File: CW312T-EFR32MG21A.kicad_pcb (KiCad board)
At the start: 2 copper layers, 58.7 x 53.7 mm, 22 parts, among them J1 1x3 straight header pins, P1 PCIEx4 EDGE CONNECTOR, U1 EFR32MG21A020F1024IM32-BR

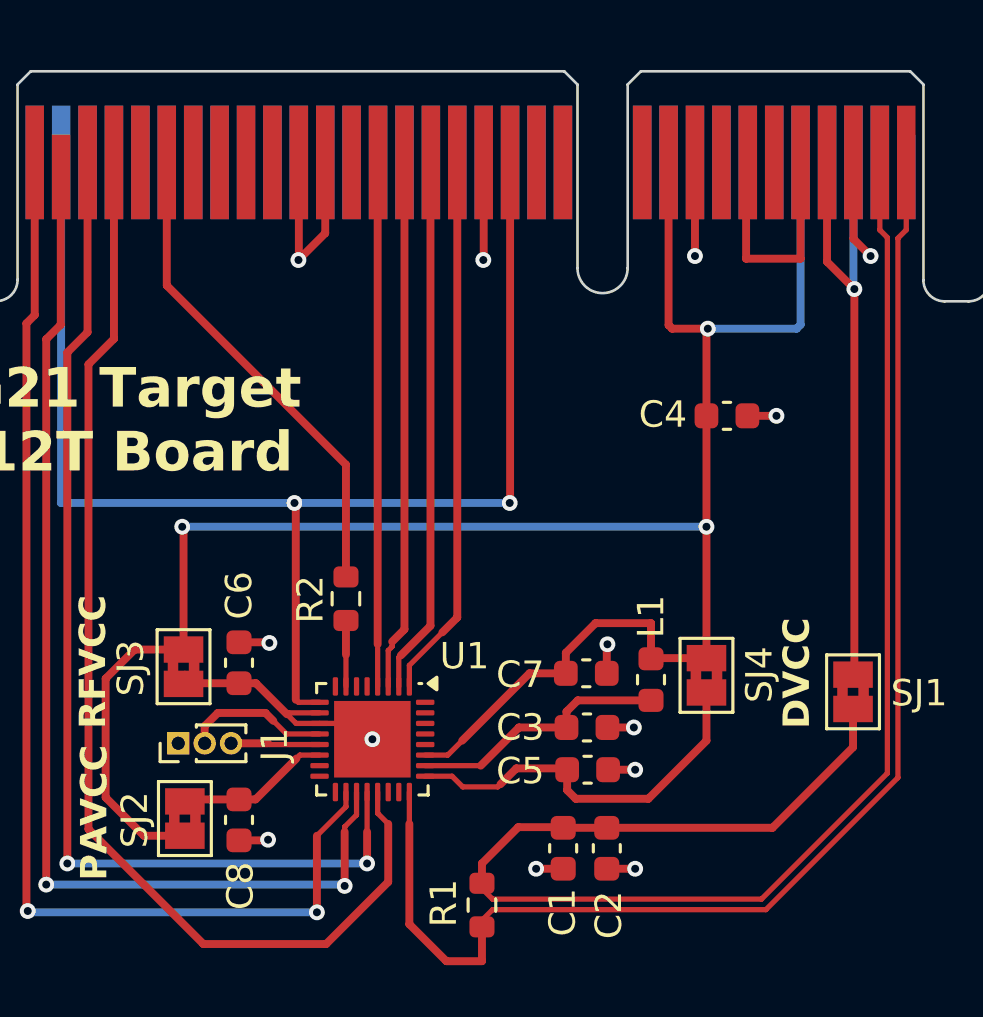
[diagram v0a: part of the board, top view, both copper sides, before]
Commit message: updated schematic to fix power, updated pcb and production files - ready for review
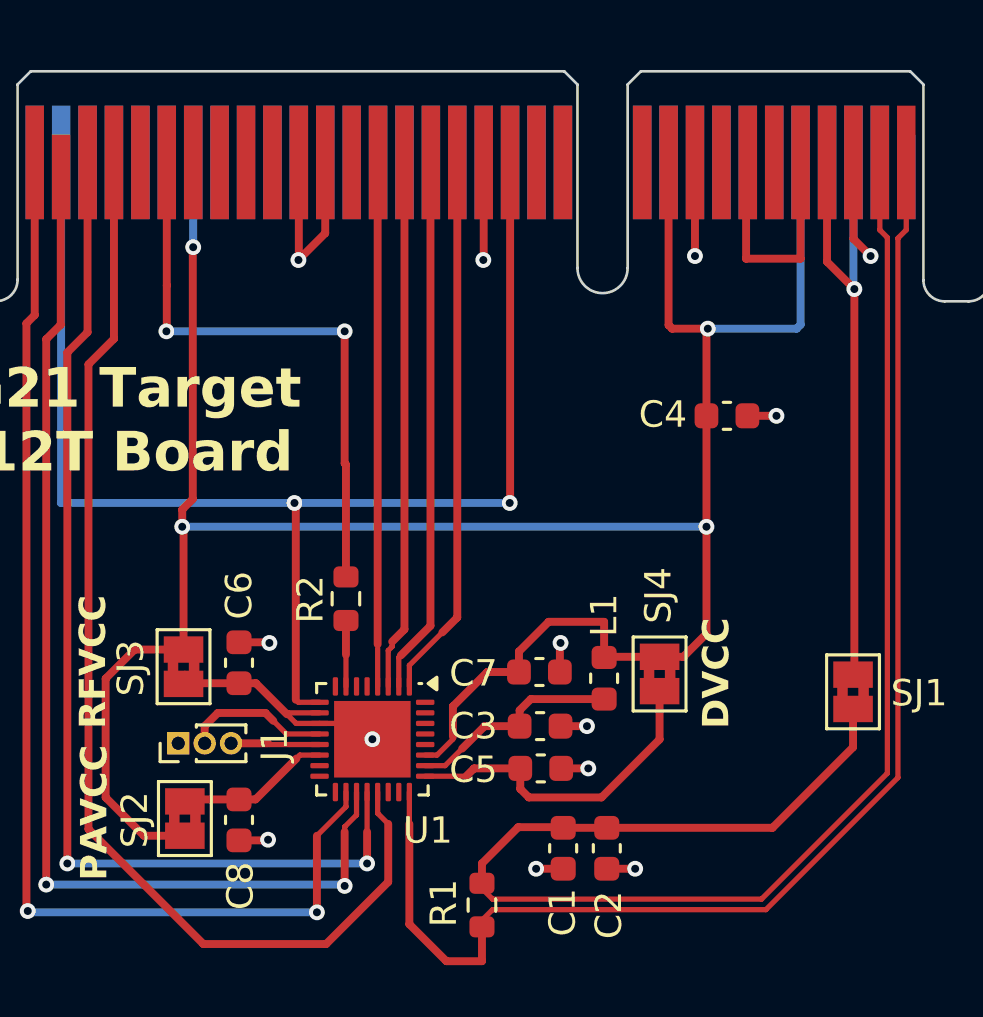
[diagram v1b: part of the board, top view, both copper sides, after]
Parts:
- moved C5 1.78 mm to (135.2, 90.3)
- moved C3 1.78 mm to (135.2, 88.8)
- moved C7 1.78 mm to (135.2, 86.7)
- moved L1 1.78 mm to (137.6, 86.9)
- moved SJ4 1.78 mm to (139.7, 86.8)
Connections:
- P1 pad A26: unconnected-(P1-JTAG_VREF-PadA26) -> +3V3
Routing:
- net +3V3: track 80.5 -> 94.6 mm, vias 3 -> 4
- net Net-(P1-CLKOUT): track 18.5 -> 22.5 mm, vias 0 -> 2
- net Net-(U1-DVDD): track 14.9 -> 12.9 mm
- net Net-(U1-AVDD): track 9.93 -> 8.17 mm

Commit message: updated silkscreen and production files
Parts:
- moved C4 1.75 mm to (142.3, 78.8)
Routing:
- net +3V3: track 94.6 -> 93.1 mm
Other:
- board text added: "+1V2"
- board text added: "+3V3"
- board text added: "Enable Supplies"
- board text added: "RST"
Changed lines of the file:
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@@
 	(footprint "Capacitor_SMD:C_0603_1608Metric"
 		(layer "F.Cu")
-		(at 142.275 77 180)
+		(at 142.35 78.75 180)
 		(descr "Capacitor SMD 0603 (1608 Metric), square (rectangular) end terminal, IPC_7351 nominal, (Body size source: IPC-SM-782 page 76, https://www.pcb-3d.com/wordpress/wp-content/uploads/ipc-sm-782a_amendment_1_and_2.pdf), generated with kicad-footprint-generator")
 		(tags "capacitor")
@@
 		)
 	)
+	(gr_line
+		(start 117.05 69.9)
+		(end 117.05 70.9)
+		(stroke
+			(width 0.15)
+			(type default)
+		)
+		(layer "B.SilkS")
+	)
 	(gr_rect
 		(start 154.75 103.2)
@@
 		(layer "F.SilkS")
 	)
+	(gr_line
+		(start 143 69.9)
+		(end 143 70.9)
+		(stroke
+			(width 0.15)
+			(type default)
+		)
+		(layer "F.SilkS")
+	)
 	(gr_rect
 		(start 154.75 105.35)
@@
 		(layer "F.SilkS")
 	)
+	(gr_line
+		(start 140.05 69.9)
+		(end 140.05 70.9)
+		(stroke
+			(width 0.15)
+			(type default)
+		)
+		(layer "F.SilkS")
+	)
 	(gr_text "NewAE Technology Inc. \nCW312T-EFR32MG21\nRoHS / Pb Free"
 		(at 131.05 88.2 0)
@@
 		)
 	)
+	(gr_text "RST"
+		(at 116.35 73.6 -90)
+		(layer "B.SilkS")
+		(effects
+			(font
+				(size 1 1)
+				(thickness 0.15)
+			)
+			(justify left bottom mirror)
+		)
+	)
 	(gr_text "B: Secure Vault"
 		(at 147.6 110.9 0)
@@
 		)
 	)
+	(gr_text "Enable Supplies"
+		(at 135.65 76.85 0)
+		(layer "F.SilkS")
+		(effects
+			(font
+				(size 1 1)
+				(thickness 0.15)
+			)
+			(justify left bottom)
+		)
+	)
 	(gr_text "DVCC"
 		(at 142.45 88.85 90)
@@
 		)
 	)
+	(gr_text "+3V3"
+		(at 139.4 71 270)
+		(layer "F.SilkS")
+		(effects
+			(font
+				(size 1 1)
+				(thickness 0.15)
+			)
+			(justify left bottom)
+		)
+	)
+	(gr_text "+1V2"
+		(at 142.35 71 270)
+		(layer "F.SilkS")
+		(effects
+			(font
+				(size 1 1)
+				(thickness 0.15)
+			)
+			(justify left bottom)
+		)
+	)
 	(gr_text "A: Std. Security"
 		(at 147.75 109.25 0)
@@
 	)
 	(segment
-		(start 143.05 77)
-		(end 144.15 77)
+		(start 143.15 78.75)
+		(end 144.25 78.75)
 		(width 0.3)
 		(layer "F.Cu")
@@
 	)
 	(via
-		(at 144.15 77)
+		(at 144.25 78.75)
 		(size 0.6)
 		(drill 0.3)
@@
 	)
 	(segment
-		(start 140.2 73.7)
-		(end 140.065 73.565)
+		(start 140.2 72.2)
+		(end 140.065 72.065)
 		(width 0.3)
 		(layer "F.Cu")
@@
 	)
 	(segment
-		(start 141.55 73.7)
-		(end 140.2 73.7)
-		(width 0.3)
-		(layer "F.Cu")
-		(net 4)
-	)
-	(segment
-		(start 141.5 73.75)
-		(end 141.55 73.7)
+		(start 141.55 72.2)
+		(end 140.2 72.2)
 		(width 0.3)
 		(layer "F.Cu")
@@
 	)
 	(segment
-		(start 141.5 77)
-		(end 141.5 73.75)
+		(start 141.5 72.25)
+		(end 141.55 72.2)
 		(width 0.3)
 		(layer "F.Cu")
@@
 	)
 	(segment
-		(start 141.5 77)
-		(end 141.5 81.2)
-		(width 0.3)
+		(start 137.649996 86.125004)
+		(end 137.625 86.15)
+		(width 0.2)
 		(layer "F.Cu")
 		(net 4)
 	)
 	(segment
-		(start 137.649996 86.125004)
-		(end 137.625 86.15)
-		(width 0.2)
+		(start 141.5 81.2)
+		(end 141.5 72.25)
+		(width 0.3)
 		(layer "F.Cu")
 		(net 4)
@@
 	)
 	(segment
-		(start 140.065 73.565)
-		(end 140.065 67.405)
+		(start 122.05 80.15)
+		(end 121.65 80.55)
 		(width 0.3)
 		(layer "F.Cu")
@@
 	)
 	(segment
-		(start 122.05 80.15)
-		(end 121.65 80.55)
+		(start 140.065 72.065)
+		(end 140.065 67.405)
 		(width 0.3)
 		(layer "F.Cu")
@@
 	)
 	(via
-		(at 141.55 73.7)
+		(at 141.55 72.2)
 		(size 0.6)
 		(drill 0.3)
@@
 	)
 	(segment
-		(start 145.065 73.55)
+		(start 145.065 72.05)
 		(end 145.065 67.405)
 		(width 0.3)
@@
 	)
 	(segment
-		(start 144.915 73.7)
-		(end 145.065 73.55)
+		(start 144.915 72.2)
+		(end 145.065 72.05)
 		(width 0.3)
 		(layer "B.Cu")
@@
 	)
 	(segment
-		(start 141.55 73.7)
-		(end 144.915 73.7)
+		(start 141.55 72.2)
+		(end 144.915 72.2)
 		(width 0.3)
 		(layer "B.Cu")
@@
 	)
 	(segment
-		(start 121.065 72.065)
-		(end 121.065 73.785)
-		(width 0.3)
-		(layer "F.Cu")
-		(net 31)
-	)
-	(segment
-		(start 127.8 78.8)
-		(end 127.85 78.85)
+		(start 127.85 73.85)
+		(end 127.85 83.1)
 		(width 0.3)
 		(layer "F.Cu")
@@
 	)
 	(segment
-		(start 121.065 73.785)
-		(end 121.05 73.8)
+		(start 121.065 72.065)
+		(end 121.065 73.785)
 		(width 0.3)
 		(layer "F.Cu")
@@
 	)
 	(segment
-		(start 127.85 78.85)
-		(end 127.85 83.1)
+		(start 127.8 73.8)
+		(end 127.85 73.85)
 		(width 0.3)
 		(layer "F.Cu")
@@
 	)
 	(segment
-		(start 127.8 73.8)
-		(end 127.8 78.8)
+		(start 121.065 73.785)
+		(end 121.05 73.8)
 		(width 0.3)
 		(layer "F.Cu")

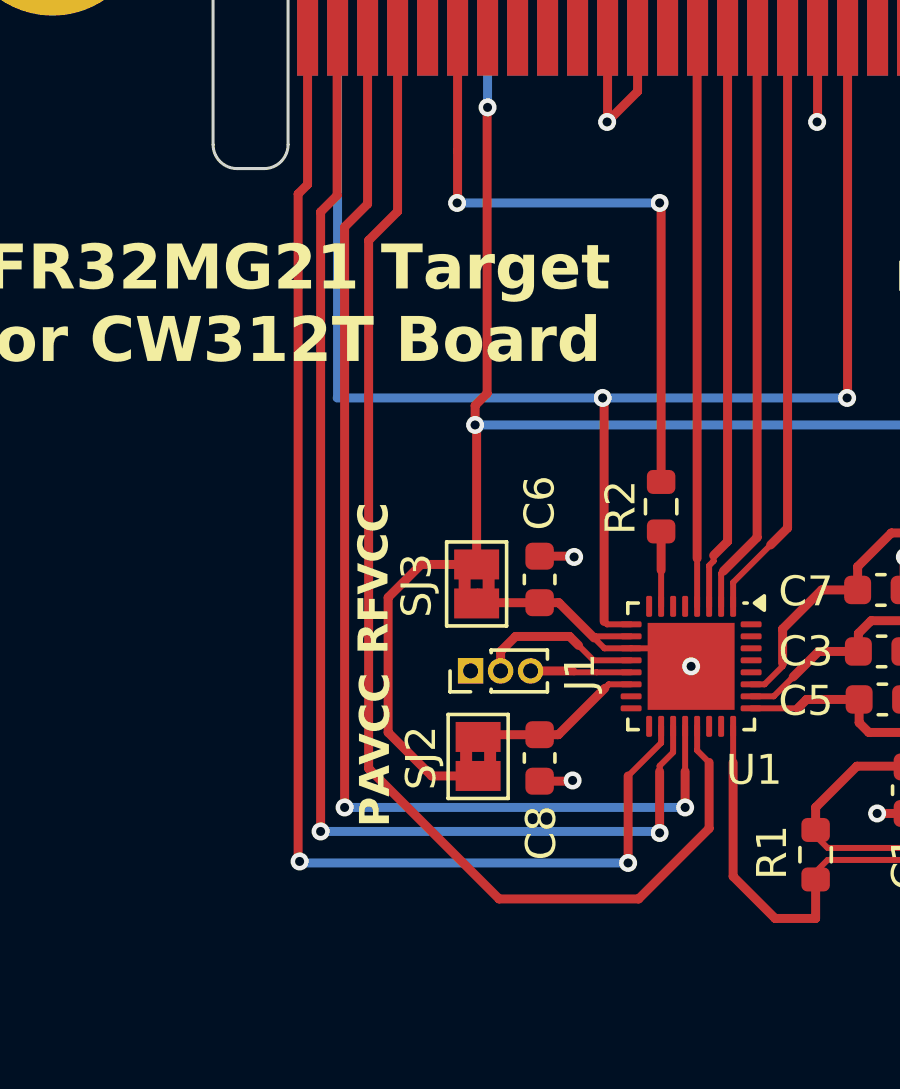
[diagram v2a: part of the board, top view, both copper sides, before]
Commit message: updated 3 pin header to fix footprint
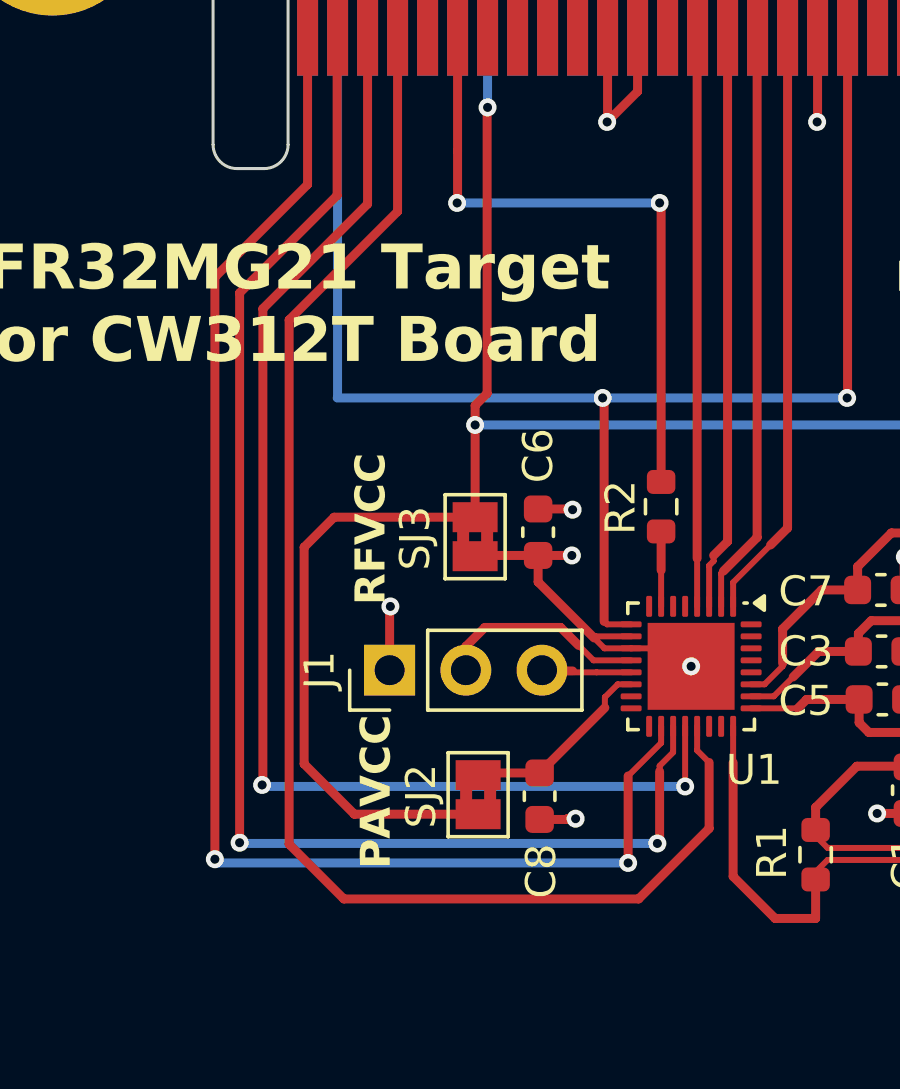
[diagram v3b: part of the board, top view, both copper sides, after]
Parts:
- J1: footprint Connector_PinHeader_1.00mm:PinHeader_1x03_P1.00mm_Vertical -> Connector_PinHeader_2.54mm:PinHeader_1x03_P2.54mm_Vertical
- moved J1 2.70 mm to (118.8, 89.4)
- moved C6 1.58 mm to (123.8, 84.8)
- moved SJ3 1.58 mm to (121.7, 84.9)
- moved C8 1.28 mm to (123.8, 93.6)
- moved SJ2 1.28 mm to (121.8, 93.5)
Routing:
- net +3V3: track 93.1 -> 99.9 mm
- net /TDI: track 43.3 -> 48.6 mm
- net GND: track 36.9 -> 41.4 mm, vias 13 -> 15
- net /SWDIO: track 42.1 -> 46.6 mm
- net /SWCLK: track 44.5 -> 48.4 mm
- net /TDO: track 40.9 -> 43.4 mm
- net Net-(U1-RF2G4_IO2): track 5.49 -> 7.02 mm
- net Net-(U1-PAVDD): track 5.83 -> 6.45 mm

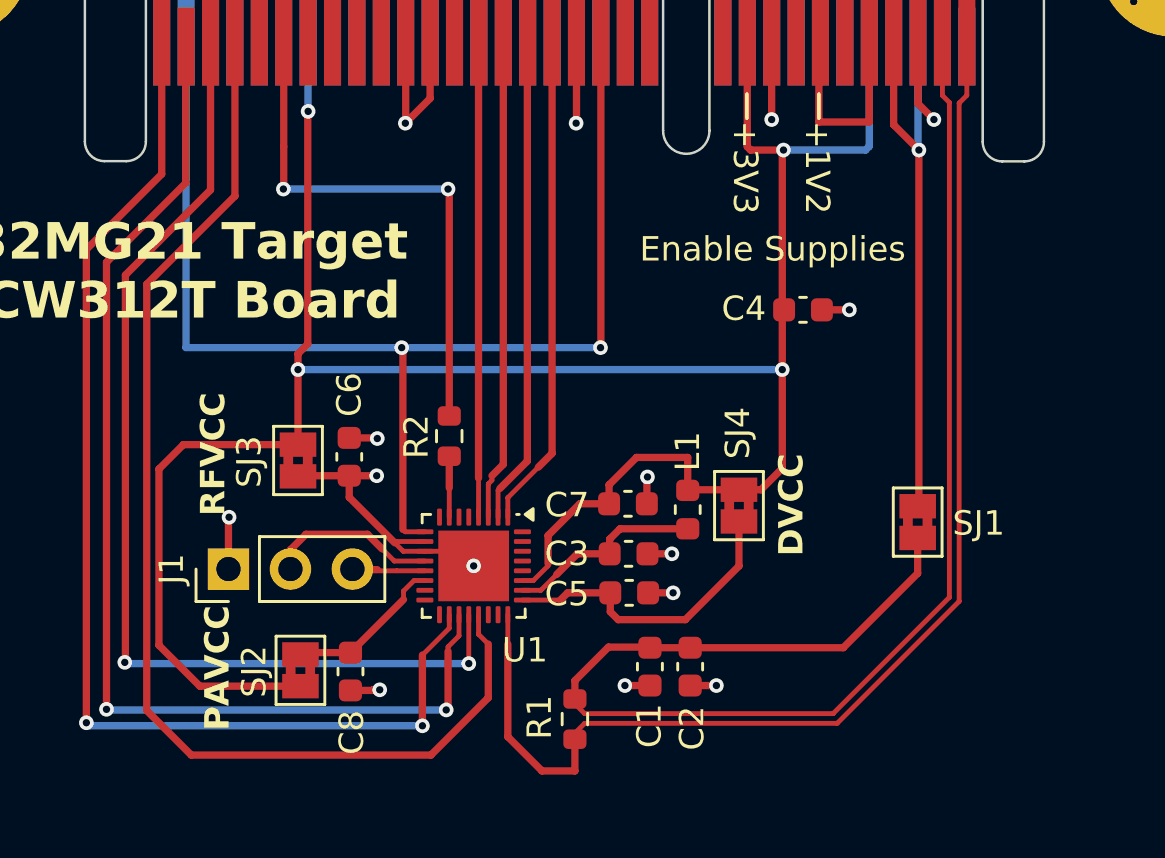
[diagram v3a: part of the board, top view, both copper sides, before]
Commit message: updated schematic and pcb after library reorganization
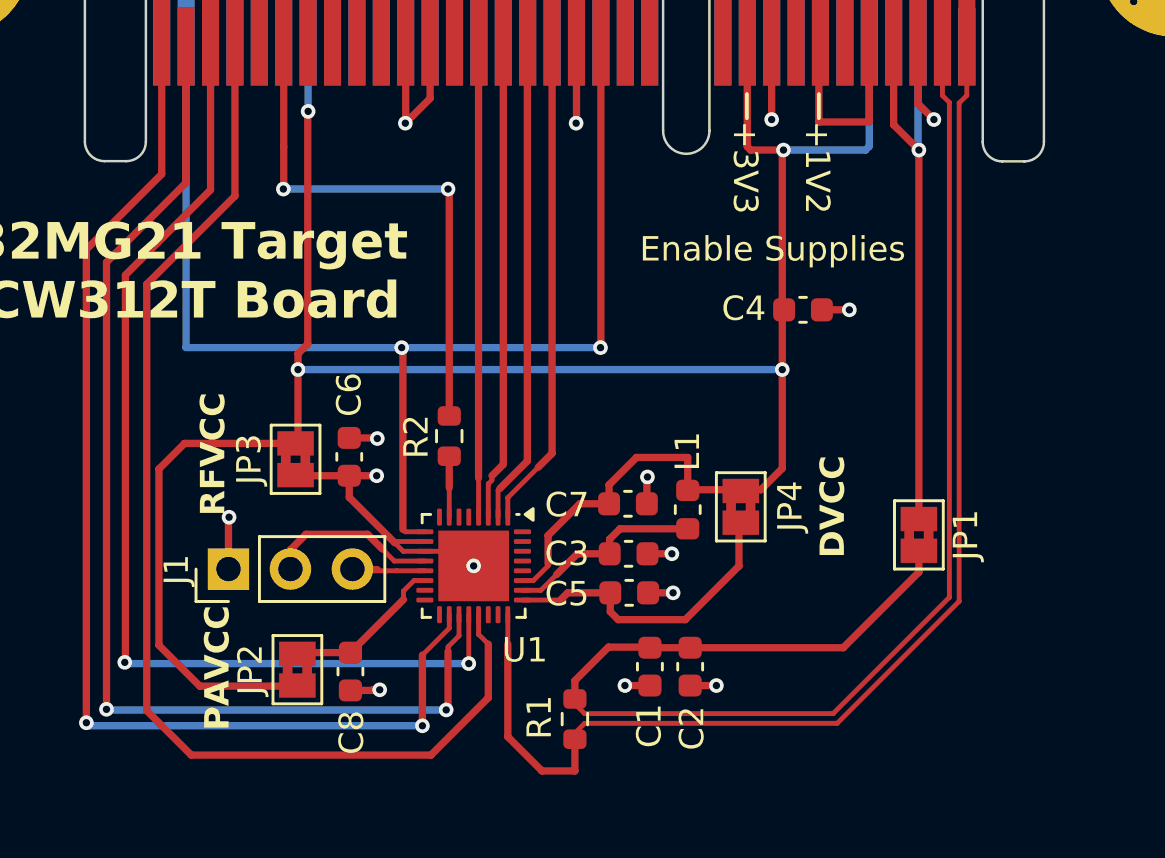
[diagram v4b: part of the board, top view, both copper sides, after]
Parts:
- removed SJ1, SJ2, SJ3, SJ4: ~, Jumper:SolderJumper-2_P1.3mm_Bridged2Bar_Pad1.0x1.5mm
- added JP1: ~, Jumper:SolderJumper-2_P1.3mm_Bridged2Bar_Pad1.0x1.5mm, F.Cu at (147.1, 88.0)
- added JP2: ~, Jumper:SolderJumper-2_P1.3mm_Bridged2Bar_Pad1.0x1.5mm, F.Cu at (121.6, 93.5)
- added JP3: ~, Jumper:SolderJumper-2_P1.3mm_Bridged2Bar_Pad1.0x1.5mm, F.Cu at (121.5, 84.9)
- added JP4: ~, Jumper:SolderJumper-2_P1.3mm_Bridged2Bar_Pad1.0x1.5mm, F.Cu at (139.8, 86.8)
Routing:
- net /FILT: track 24.6 -> 25.2 mm
- net /SHUNTH: track 59.2 -> 58.6 mm
